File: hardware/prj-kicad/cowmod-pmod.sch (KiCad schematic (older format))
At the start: 9 parts, among them J1 JUMPER, Q11 SI2319C, Q12 SQ2318, U11 TXS0108E-PW

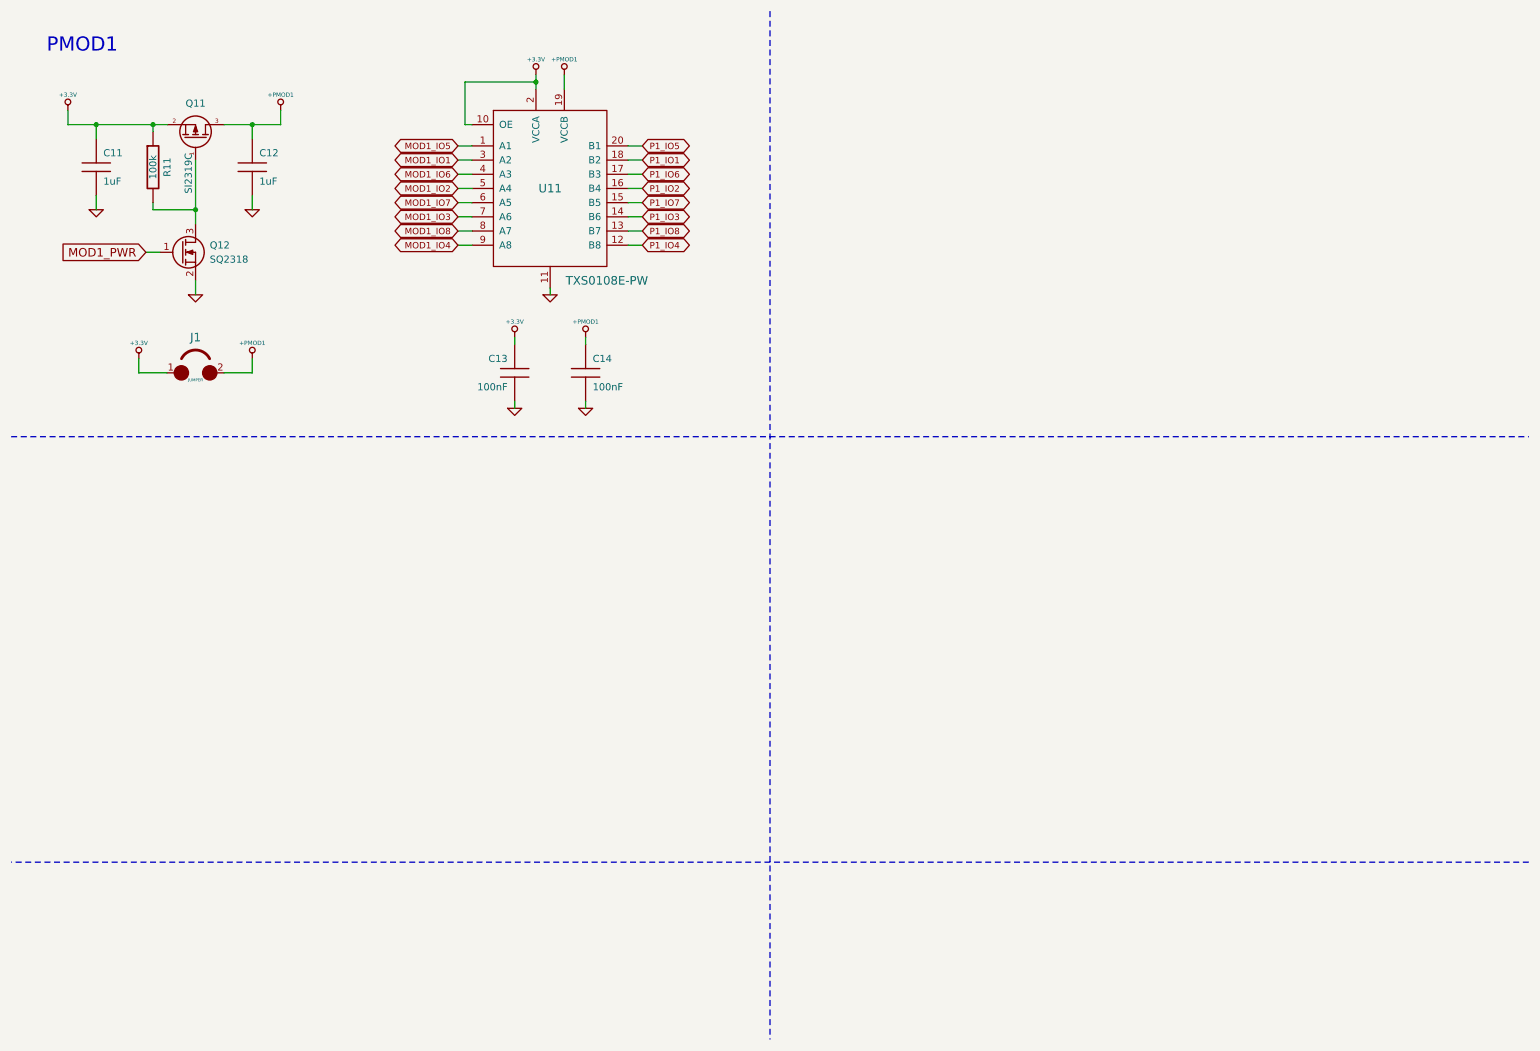
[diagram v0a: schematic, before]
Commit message: = ADD: Insert FPGA and route all PMOD ports
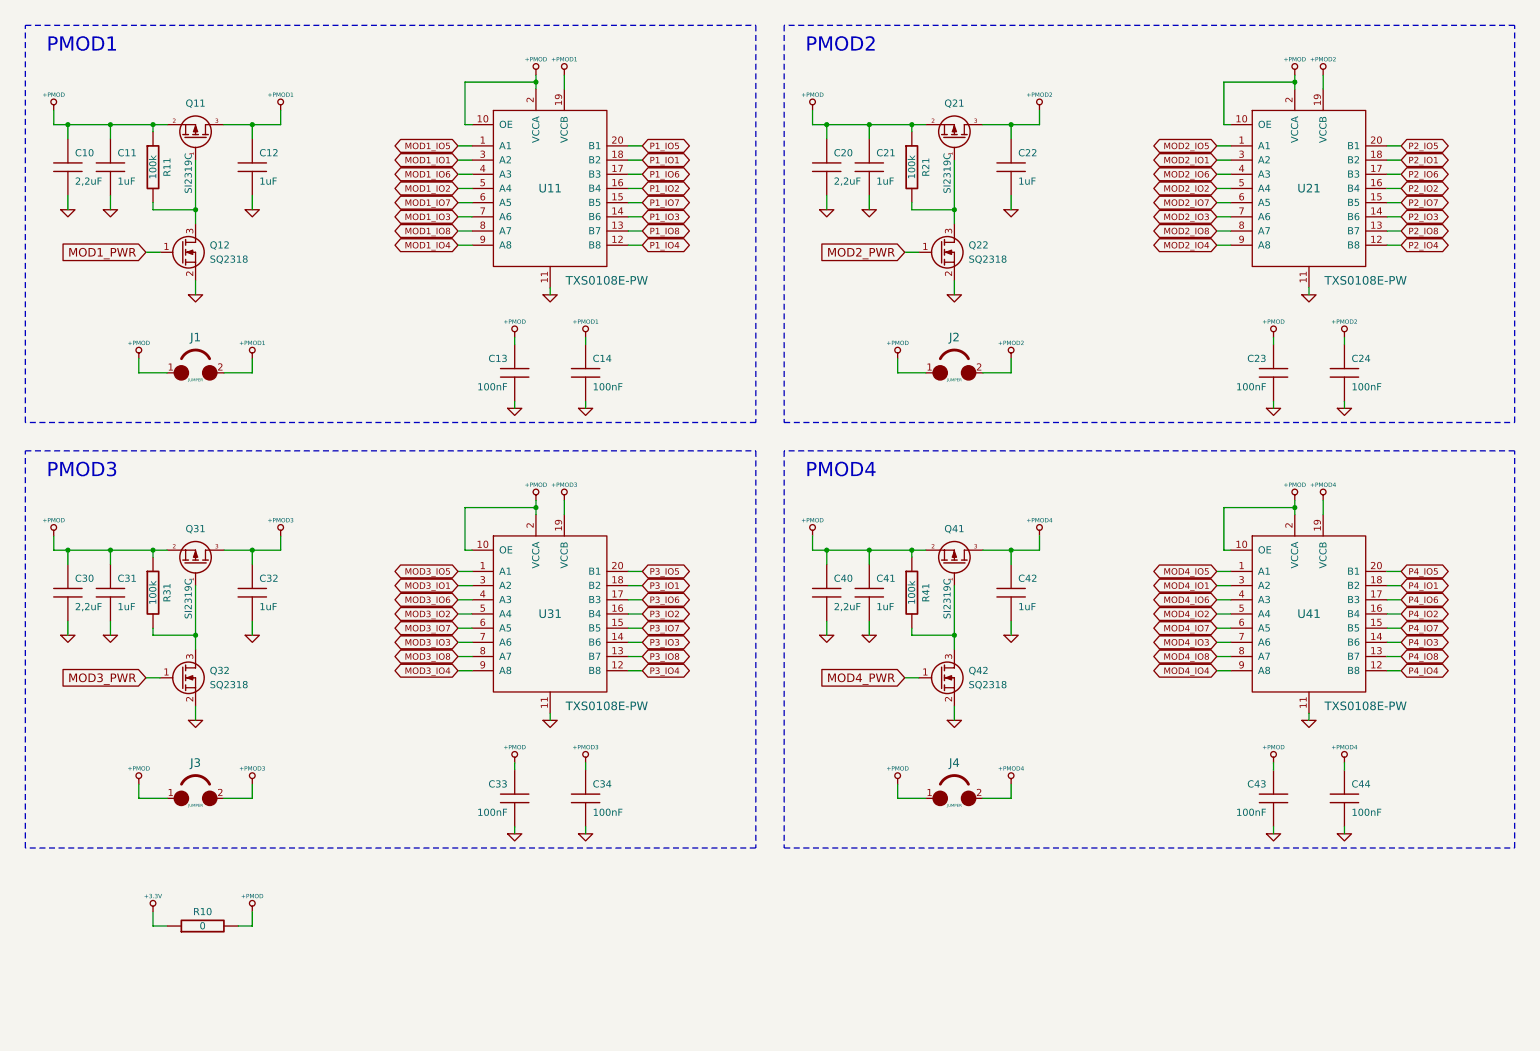
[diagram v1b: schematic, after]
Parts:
- added C10, C20, C30, C40: 2,2uF, cowmod:SMD1210, symbol C
- added C21, C31, C41: 1uF, cowmod:SMD0603, symbol C
- added C22, C32, C42: 1uF, cowmod:SMD0805, symbol C
- added C23, C24, C33, C34, C43, C44: 100nF, cowmod:SMD0603, symbol C
- added J2, J3, J4: JUMPER, cowmod:CONN_2, symbol JUMPER
- added Q21, Q31, Q41: SI2319C, cowmod:SOT23-3, symbol Q_PMOS
- added Q22, Q32, Q42: SQ2318, cowmod:SOT23-3, symbol Q_NMOS
- added R10: 0, cowmod:SMD0805, symbol R
- added R21, R31, R41: 100k, cowmod:SMD0603, symbol R
- added U21, U31, U41: TXS0108E-PW, cowmod:TSSOP20, symbol TXS0108E-PW
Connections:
- net +3.3V: now also R10.1; no longer C11.1, C13.1, J1.1, Q11.2 (S), R11.1, U11.10 (OE), U11.2 (VCCA)
- net GND: now also C10.2, C20.2, C21.2, C22.2, C23.2, C24.2, C30.2, C31.2, C32.2, C33.2, C34.2, C40.2, C41.2, C42.2, C43.2, C44.2, Q22.2 (S), Q32.2 (S), Q42.2 (S), U21.11, U31.11, U41.11
- new net: Q21.1 (G), Q22.3 (D), R21.2
- new net: Q31.1 (G), Q32.3 (D), R31.2
- new net: Q41.1 (G), Q42.3 (D), R41.2
- new net +PMOD: C10.1, C11.1, C13.1, C20.1, C21.1, C23.1, C30.1, C31.1, C33.1, C40.1, C41.1, C43.1, J1.1, J2.1, J3.1, J4.1, Q11.2 (S), Q21.2 (S), Q31.2 (S), Q41.2 (S), R10.2, R11.1, R21.1, R31.1, R41.1, U11.10 (OE), U11.2 (VCCA), U21.10 (OE), U21.2 (VCCA), U31.10 (OE), U31.2 (VCCA), U41.10 (OE), U41.2 (VCCA)
- new net +PMOD2: C22.1, C24.1, J2.2, Q21.3 (D), U21.19 (VCCB)
- new net +PMOD3: C32.1, C34.1, J3.2, Q31.3 (D), U31.19 (VCCB)
- new net +PMOD4: C42.1, C44.1, J4.2, Q41.3 (D), U41.19 (VCCB)
- new net MOD2_IO1: U21.3 (A2)
- new net MOD2_IO2: U21.5 (A4)
- new net MOD2_IO3: U21.7 (A6)
- new net MOD2_IO4: U21.9 (A8)
- new net MOD2_IO5: U21.1 (A1)
- new net MOD2_IO6: U21.4 (A3)
- new net MOD2_IO7: U21.6 (A5)
- new net MOD2_IO8: U21.8 (A7)
- new net MOD2_PWR: Q22.1 (G)
- new net MOD3_IO1: U31.3 (A2)
- new net MOD3_IO2: U31.5 (A4)
- new net MOD3_IO3: U31.7 (A6)
- new net MOD3_IO4: U31.9 (A8)
- new net MOD3_IO5: U31.1 (A1)
- new net MOD3_IO6: U31.4 (A3)
- new net MOD3_IO7: U31.6 (A5)
- new net MOD3_IO8: U31.8 (A7)
- new net MOD3_PWR: Q32.1 (G)
- new net MOD4_IO1: U41.3 (A2)
- new net MOD4_IO2: U41.5 (A4)
- new net MOD4_IO3: U41.7 (A6)
- new net MOD4_IO4: U41.9 (A8)
- new net MOD4_IO5: U41.1 (A1)
- new net MOD4_IO6: U41.4 (A3)
- new net MOD4_IO7: U41.6 (A5)
- new net MOD4_IO8: U41.8 (A7)
- new net MOD4_PWR: Q42.1 (G)
- new net P2_IO1: U21.18 (B2)
- new net P2_IO2: U21.16 (B4)
- new net P2_IO3: U21.14 (B6)
- new net P2_IO4: U21.12 (B8)
- new net P2_IO5: U21.20 (B1)
- new net P2_IO6: U21.17 (B3)
- new net P2_IO7: U21.15 (B5)
- new net P2_IO8: U21.13 (B7)
- new net P3_IO1: U31.18 (B2)
- new net P3_IO2: U31.16 (B4)
- new net P3_IO3: U31.14 (B6)
- new net P3_IO4: U31.12 (B8)
- new net P3_IO5: U31.20 (B1)
- new net P3_IO6: U31.17 (B3)
- new net P3_IO7: U31.15 (B5)
- new net P3_IO8: U31.13 (B7)
- new net P4_IO1: U41.18 (B2)
- new net P4_IO2: U41.16 (B4)
- new net P4_IO3: U41.14 (B6)
- new net P4_IO4: U41.12 (B8)
- new net P4_IO5: U41.20 (B1)
- new net P4_IO6: U41.17 (B3)
- new net P4_IO7: U41.15 (B5)
- new net P4_IO8: U41.13 (B7)
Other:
- note added: "PMOD2"
- note added: "PMOD3"
- note added: "PMOD4"
- moved on the sheet: C11
